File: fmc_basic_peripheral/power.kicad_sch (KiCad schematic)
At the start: 27 parts, among them U13 MT2492, U4 AIP74LVC1T45GB236TR, U5 GX0011D

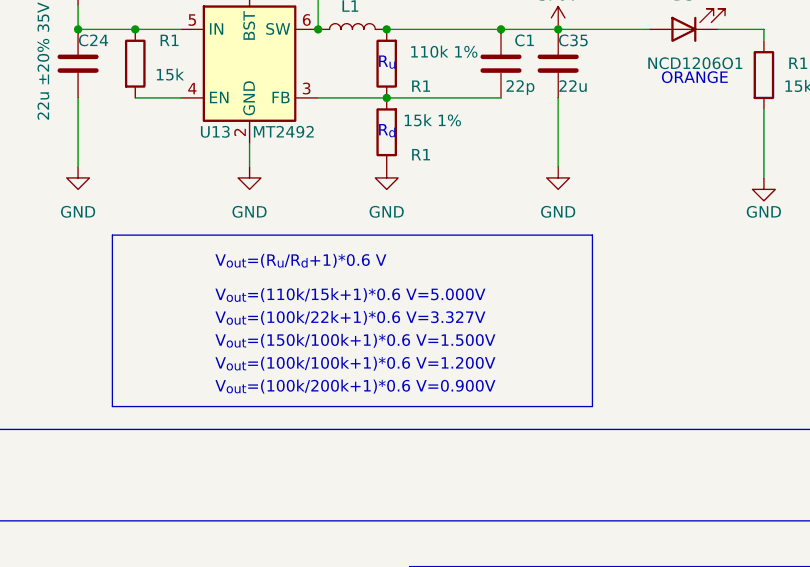
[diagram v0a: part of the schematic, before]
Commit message: power.kicad_sch: add formula for 1.8V voltage
Signed-off-by: Huang Rui <vowstar@gmail.com>
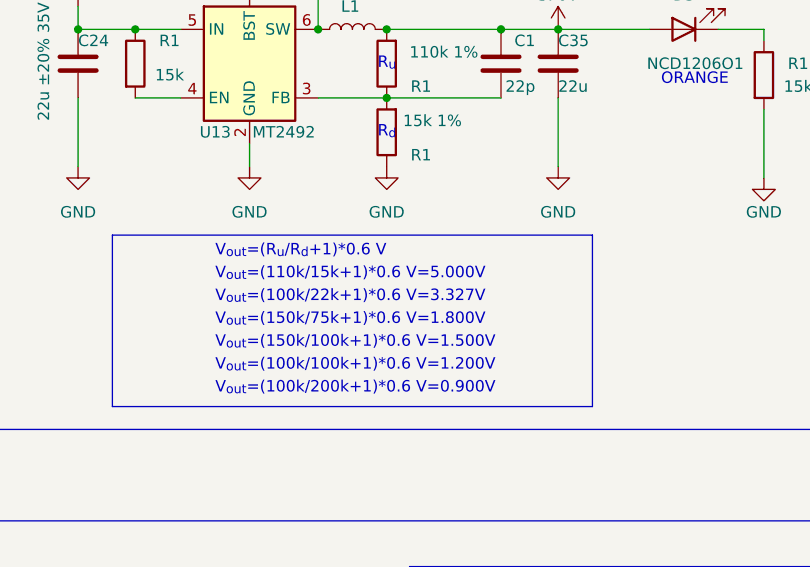
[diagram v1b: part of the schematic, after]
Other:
- note added: "V_{out}=(150k/75k+1)*0.6 V=1.800V"
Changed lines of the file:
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@@
     (effects (font (size 1.27 1.27) (color 194 0 0 1)) (justify left bottom))
   )
-  (text "V_{out}=(100k/22k+1)*0.6 V=3.327V " (at 148.59 68.58 0)
+  (text "V_{out}=(100k/22k+1)*0.6 V=3.327V " (at 148.59 66.04 0)
     (effects (font (size 1.27 1.27)) (justify left bottom))
   )
@@
     (effects (font (size 1.27 1.27)) (justify left bottom))
   )
-  (text "V_{out}=(110k/15k+1)*0.6 V=5.000V " (at 148.59 66.04 0)
+  (text "V_{out}=(110k/15k+1)*0.6 V=5.000V " (at 148.59 63.5 0)
     (effects (font (size 1.27 1.27)) (justify left bottom))
   )
@@
     (effects (font (size 1.27 1.27)) (justify left bottom))
   )
-  (text "V_{out}=(R_{u}/R_{d}+1)*0.6 V" (at 148.59 62.23 0)
+  (text "V_{out}=(R_{u}/R_{d}+1)*0.6 V" (at 148.59 60.96 0)
     (effects (font (size 1.27 1.27)) (justify left bottom))
   )
@@
     (effects (font (size 1.27 1.27)) (justify left bottom))
   )
+  (text "V_{out}=(150k/75k+1)*0.6 V=1.800V " (at 148.59 68.58 0)
+    (effects (font (size 1.27 1.27)) (justify left bottom))
+  )

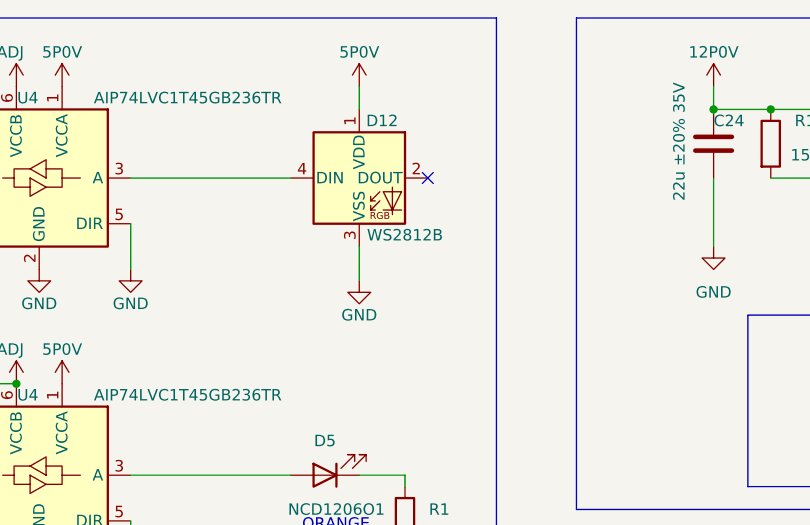
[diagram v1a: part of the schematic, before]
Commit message: {*.kicad_pcb,power.kicad_sch}: Optimize the silk screen of WS2812
Optimize the silk screen of WS2812 to avoid mistakes by SMT engineers

Signed-off-by: Huang Rui <vowstar@gmail.com>
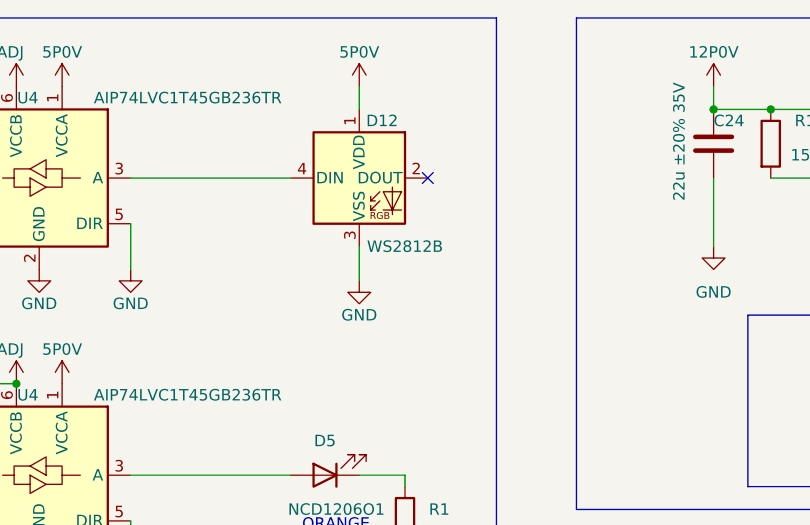
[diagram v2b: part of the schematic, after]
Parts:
- D12: footprint LED_SMD:LED_WS2812B_PLCC4_5.0x5.0mm_P3.2mm -> CHIPSAlliance_LED:LED_WS2812B_PLCC4_5.0x5.0mm_P3.2mm; symbol LED:WS2812B -> CHIPSAlliance_LED:WS2812B
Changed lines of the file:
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@@
     )
   )
-  (symbol (lib_id "LED:WS2812B") (at 93.98 43.18 0) (unit 1)
+  (symbol (lib_id "CHIPSAlliance_LED:WS2812B") (at 88.9 38.1 0) (unit 1)
     (in_bom yes) (on_board yes) (dnp no)
     (property "Reference" "D12" (at 96.52 36.83 0)
       (effects (font (size 1.27 1.27)))
     )
-    (property "Value" "WS2812B" (at 99.06 49.53 0)
+    (property "Value" "WS2812B" (at 99.06 50.8 0)
       (effects (font (size 1.27 1.27)))
     )
-    (property "Footprint" "LED_SMD:LED_WS2812B_PLCC4_5.0x5.0mm_P3.2mm" (at 95.25 50.8 0)
+    (property "Footprint" "CHIPSAlliance_LED:LED_WS2812B_PLCC4_5.0x5.0mm_P3.2mm" (at 88.9 52.07 0)
       (effects (font (size 1.27 1.27)) (justify left top) hide)
     )
-    (property "Datasheet" "https://atta.szlcsc.com/upload/public/pdf/source/20200615/C114586_26EB6813EC9F2A3F6C7FBB2AD75DE01F.pdf" (at 96.52 52.705 0)
+    (property "Datasheet" "https://atta.szlcsc.com/upload/public/pdf/source/20200615/C114586_26EB6813EC9F2A3F6C7FBB2AD75DE01F.pdf" (at 88.9 54.61 0)
       (effects (font (size 1.27 1.27)) (justify left top) hide)
     )

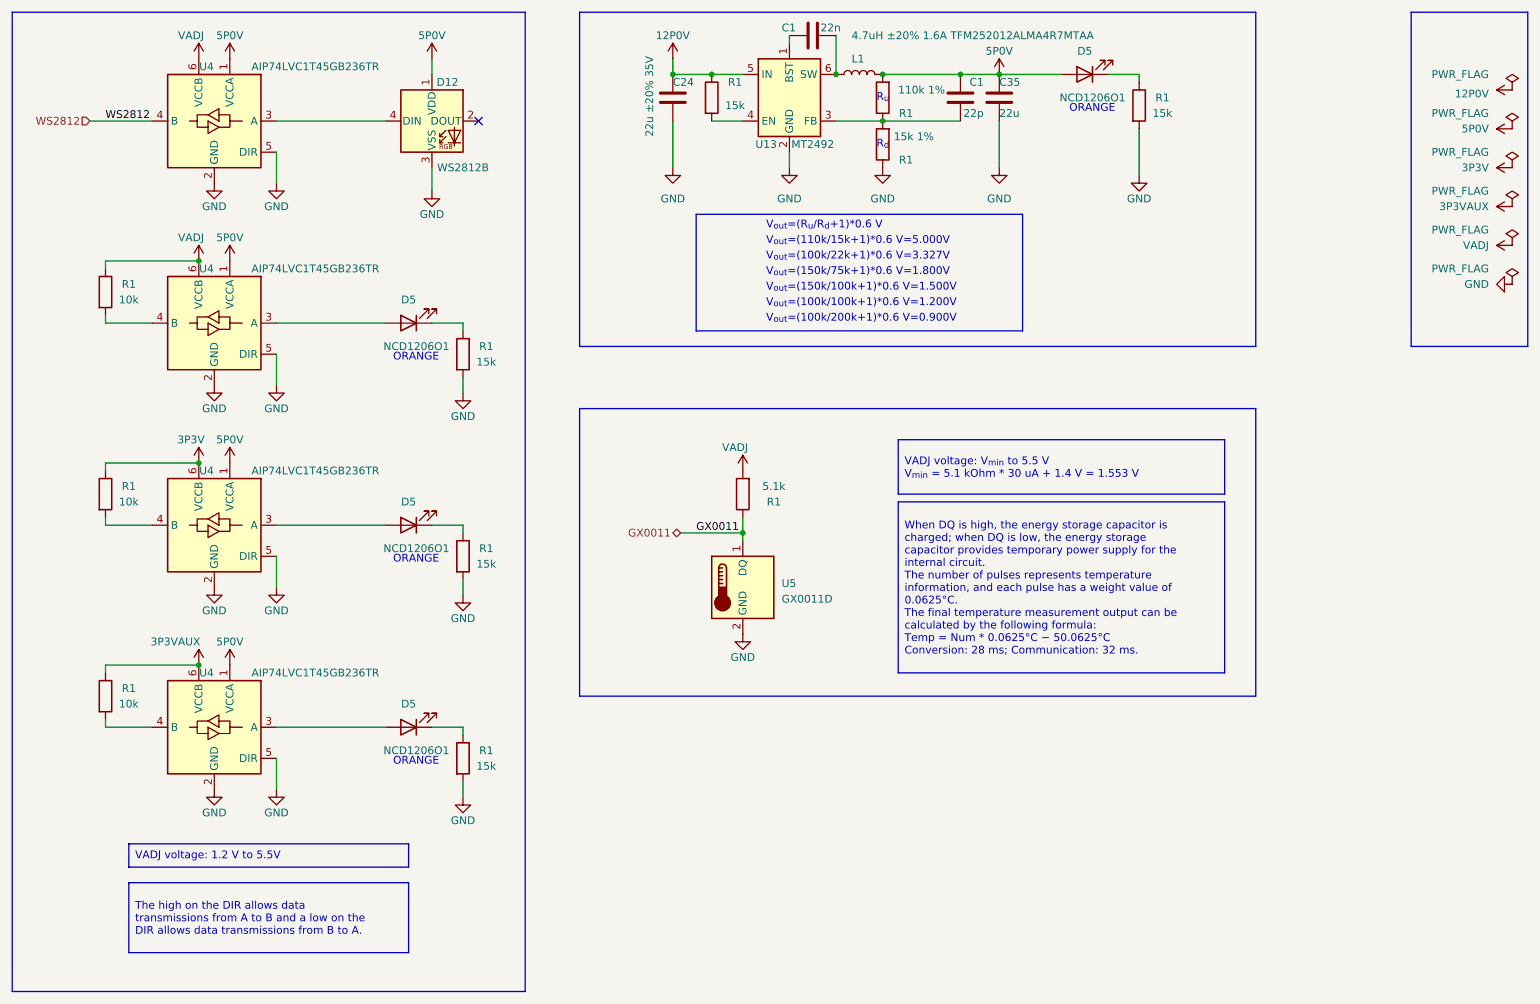
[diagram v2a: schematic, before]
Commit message: *.kicad_sch: fix jtag connection
- remove ws2812
- remove GX0011

Signed-off-by: Huang Rui <vowstar@gmail.com>
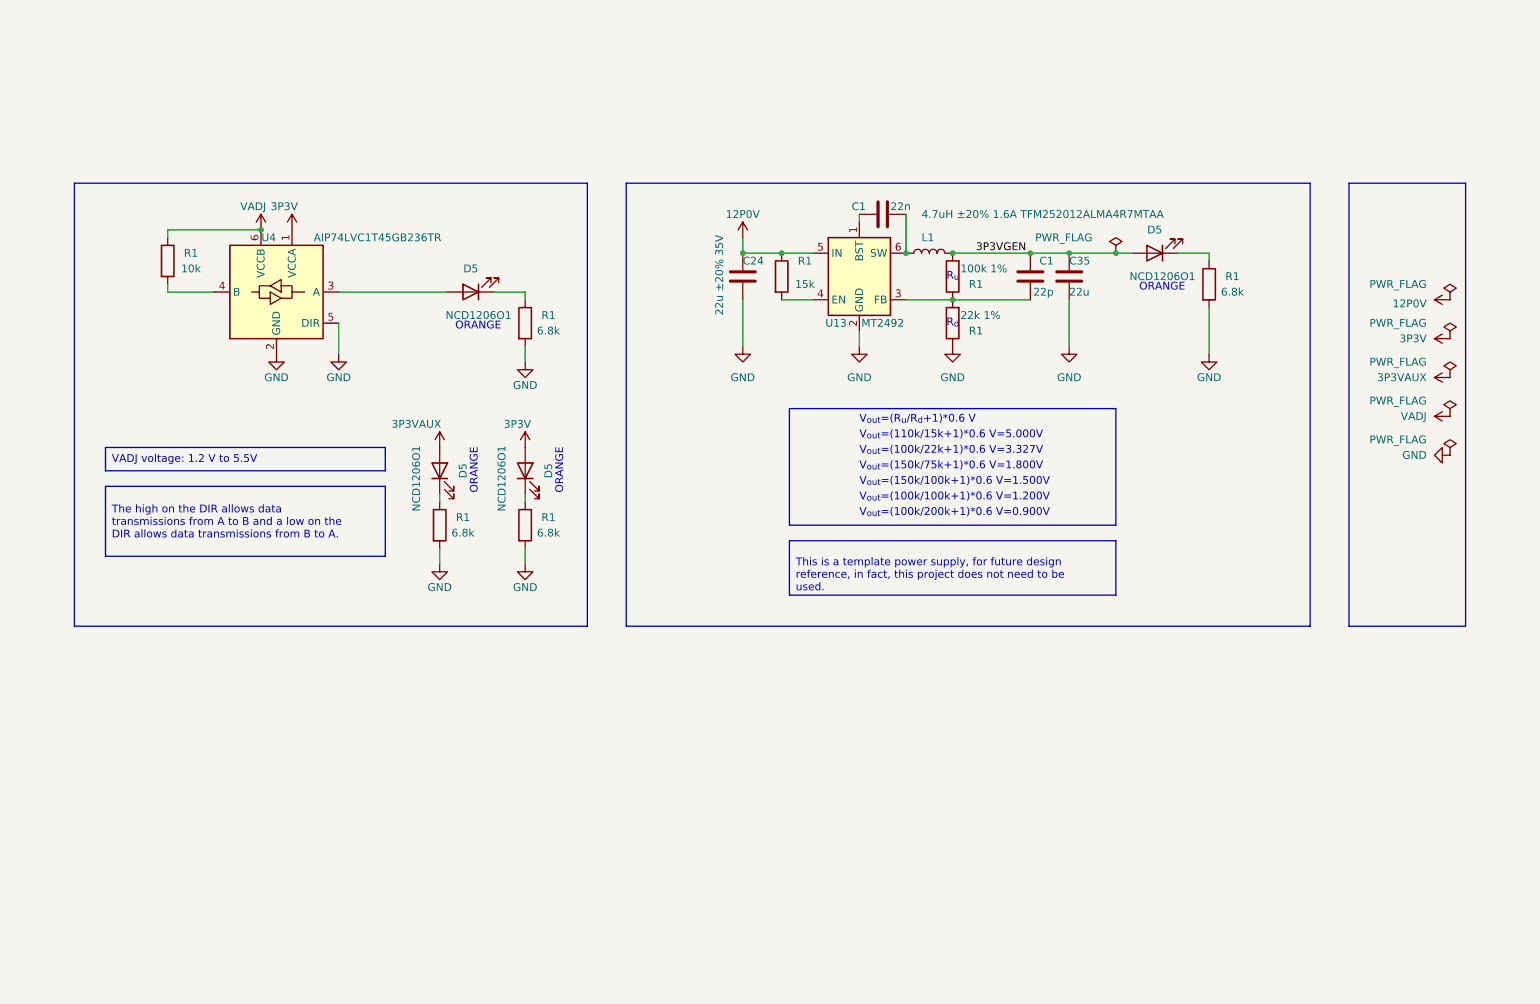
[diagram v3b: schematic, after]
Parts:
- removed D12: WS2812B, CHIPSAlliance_LED:LED_WS2812B_PLCC4_5.0x5.0mm_P3.2mm, symbol CHIPSAlliance_LED:WS2812B
- removed R1: 5.1k, Resistor_SMD:R_0402_1005Metric, symbol Device:R
- removed R1 (x2): 10k, Resistor_SMD:R_0402_1005Metric, symbol Device:R
- removed U4 (x3): AIP74LVC1T45GB236TR, Package_TO_SOT_SMD:SOT-23-6, symbol CHIPSAlliance_Logic:AIP74LVC1T45GB236TR
- removed U5: GX0011D, CHIPSAlliance_Sensor:DFN_2L_1.6x0.8mm_P0.85mm_L, symbol CHIPSAlliance_Sensor:GX0011D
- R1: value 15k 1% -> 22k 1%
- R1: value 15k -> 6.8k
- R1: value 110k 1% -> 100k 1%
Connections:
- net 3P3V: now also D5.2 (A), U4.1 (VCCA)
- net 3P3VAUX: now also D5.2 (A)
- net 5P0V renamed 3P3VGEN
- net 3P3VGEN: no longer U4.1 (VCCA)
- no-connect marks 1 -> 0
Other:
- moved on the sheet: C1, C24, C35, D5, L1, R1, U13, U4
